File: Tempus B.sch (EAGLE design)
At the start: 37 parts, among them J1 PJ-102A, J2 AVR ISP, J3 GPS, J4 5-1814832-1, U1 ATTINY85-20SU, U2 HT16K33-28SOP, U3 FGPMMOPA6H, U5 DS3231MZ+, U6 L4931CZ33, U7 LM75BIM

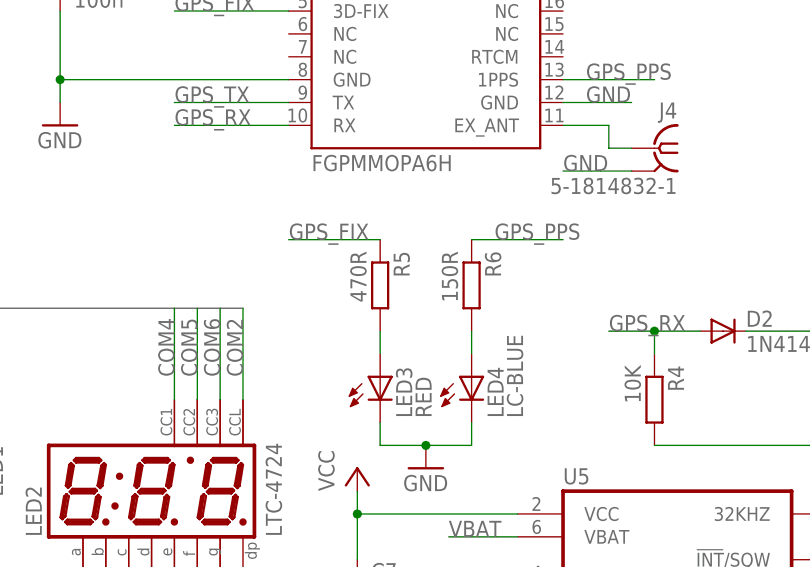
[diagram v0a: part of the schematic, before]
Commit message: Tweaking LED resistor values
After testing with the LEDs I ordered, it turns out we need a really
tiny current (0.5mA to 1mA) for the LEDs.
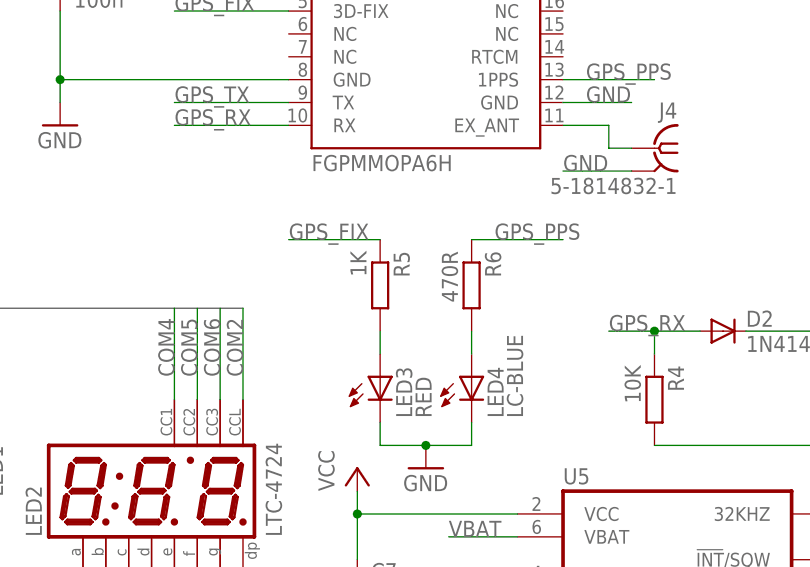
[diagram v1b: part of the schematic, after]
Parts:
- R5: value 470R -> 1K
- R6: value 150R -> 470R
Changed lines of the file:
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@@
 <part name="LED3" library="led" deviceset="LED" device="CHIPLED_1206" value="RED"/>
 <part name="LED4" library="led" deviceset="LED" device="CHIPLED_1206" value="LC-BLUE"/>
-<part name="R5" library="rcl" deviceset="R-EU_" device="R1206" value="470R"/>
-<part name="R6" library="rcl" deviceset="R-EU_" device="R1206" value="150R"/>
+<part name="R5" library="rcl" deviceset="R-EU_" device="R1206" value="1K"/>
+<part name="R6" library="rcl" deviceset="R-EU_" device="R1206" value="470R"/>
 <part name="GND11" library="supply1" deviceset="GND" device=""/>
 <part name="C9" library="rcl" deviceset="CPOL-EU" device="E2-5" value="100u"/>
